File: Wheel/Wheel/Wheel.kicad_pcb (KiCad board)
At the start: 2 copper layers, 122 parts, among them J1 Conn_02x09_Odd_Even, J10 RJ45, J11 Screw_Terminal_01x02, J12 DS-201, J13 Conn_01x04, J14 Conn_02x13_Top_Bottom, J15 DB25_Female, J16 Conn_01x06, J17 Conn_01x07, J18 Conn_01x05, J19 RJ45, J2 RJ45, J20 DB9_Male, J21 DB9_Female, J3 RJ45, J4 RJ45, J5 USB_B, J6 Conn_02x09_Odd_Even, J7 Conn_02x10_Odd_Even, J8 RJ45, J9 RJ45, U1 MCP23S17_SP, U10 PC817, U11 PC817, U12 IP4220CZ6, U13 IP4220CZ6, U14 LTC2644, U15 PC817, U16 IP4220CZ6, U17 IP4220CZ6, U2 STM32F407VETx, U3 USBLC6-2SC6, U4 IP4220CZ6, U5 IP4220CZ6, U6 AMS1117, U7 4N35, U8 PC817, U9 PC817, Y2 8MHz

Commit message: I've modified wheel's PCB
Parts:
- removed C24, C26: 104, Capacitor_SMD:C_0805_2012Metric
- removed U14: LTC2644, Package_SO:MSOP-12_3x4mm_P0.65mm
- added JP1: SolderJumper_2_Bridged, Jumper:SolderJumper-2_P1.3mm_Bridged_RoundedPad1.0x1.5mm, B.Cu at (120.7, 108.0)
- added N1: G313, cases:CASE_G313, F.Cu at (25.5, 19.5)
- C11, C13, C14, C17, JP6: moved to B.Cu
- moved D4 226.4 mm to (32.4, 65.0), turned to 270 degrees
- moved R5 225.3 mm to (37.5, 65.1), turned to 90 degrees
- moved J8 218.6 mm to (42.6, 48.1), turned to 270 degrees
- moved D5 212.8 mm to (32.4, 89.8), turned to 270 degrees
- moved R11 211.7 mm to (37.5, 89.9), turned to 90 degrees
- moved U3 211.6 mm to (70.1, 44.3)
- moved C10 211.6 mm to (59.3, 44.2)
- moved C12 211.6 mm to (55.8, 44.2)
- moved C18 211.6 mm to (60.8, 58.3)
- moved C19 211.6 mm to (55.8, 58.3)
- moved J5 211.6 mm to (62.0, 40.0)
- moved R6 211.6 mm to (64.3, 48.7)
- moved R8 211.6 mm to (71.0, 48.7)
- moved R9 211.6 mm to (67.8, 48.7)
- moved U6 211.6 mm to (58.3, 51.2)
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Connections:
- net Net-(D8-Pad2) renamed PWR_IN
- J14 pad 2: SM1 -> (no net)
- J14 pad 3: PWR -> (no net)
- J14 pad 9: DM1 -> (no net)
- J15 pad 14: SM1 -> (no net)
- J15 pad 5: DM1 -> (no net)
- J15 pad 6: (no net) -> DRIVE_SigIn1
- J18 pad 1: 3V -> GND
- J18 pad 2: GND -> 3V
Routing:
- net PWR: track 64.5 -> 144.9 mm
- net SM1: track 64.6 -> 0.00 mm, vias 2 -> 0
- net DRIVE_PA-: track 27.1 -> 91.7 mm, vias 0 -> 3
- net DRIVE_SigIn1: track 0.00 -> 54.8 mm, vias 0 -> 3
- net DRIVE_PA+: track 24.1 -> 74.8 mm, vias 0 -> 2
- net DM1: track 37.0 -> 0.00 mm, vias 2 -> 0
- net DRIVE_PB+: track 30.3 -> 66.2 mm, vias 0 -> 3
- net DRIVE_PZ-: track 36.5 -> 63.1 mm, vias 0 -> 2
- net DRIVE_PB-: track 33.4 -> 58.1 mm, vias 0 -> 2
- net PWR_IN: track 0.00 -> 23.5 mm
- net DRIVE_VREF: track 77.2 -> 55.7 mm, vias 2 -> 3
- net DRIVE_SigIn2: track 39.1 -> 56.3 mm, vias 2 -> 3
- net PEDAL_BREAK: track 0.00 -> 15.9 mm, vias 0 -> 2
- net DRIVE_PZ+: track 39.6 -> 52.5 mm, vias 0 -> 3
- net Net-(J13-Pad2): track 0.00 -> 12.6 mm
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- added copper zone on B.Cu, net COM
- added copper zone on F.Cu, net COM
- added copper zone on B.Cu, net GND
- added copper zone on F.Cu, net GND
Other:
- board outline added: 188 x 356 mm
- net class DIGITAL: clearance 0.2 -> 0.3
- net class POWER: clearance 0.5 -> 0.3
- board text added: "G1208"

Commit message: TDD Wheel's was changed
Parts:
- removed C16, C22, C27, C28: 104, Capacitor_SMD:C_0805_2012Metric
- removed R12: 330, Resistor_SMD:R_0805_2012Metric
- removed U13, U16, U17: IP4220CZ6, Package_SO:TSOP-6_1.65x3.05mm_P0.95mm
- added C3: 6pF, Capacitor_SMD:C_0805_2012Metric, F.Cu at (106.7, 68.3)
- added C4: 6pF, Capacitor_SMD:C_0805_2012Metric, F.Cu at (106.7, 60.6)
- added R4: 10M, Resistor_SMD:R_0805_2012Metric, F.Cu at (106.7, 64.4)
- added R7: 330, Resistor_SMD:R_0805_2012Metric, F.Cu at (37.5, 89.9)
- added Y1: 32,768 кГц, Crystal:Crystal_C26-LF_D2.1mm_L6.5mm_Horizontal_1EP_style2, F.Cu at (108.6, 65.4)
- C13: moved to F.Cu
- C15, C21, R6, U12, U4: moved to B.Cu
- D8: value 1N4003 -> 1N5818
- J1, J6: footprint Connector_PinHeader_2.54mm:PinHeader_2x09_P2.54mm_Vertical -> Connector_PinHeader_2.54mm:PinHeader_1x18_P2.54mm_Vertical
- J18: value Conn_01x05 -> Conn_01x06; footprint Connector_PinHeader_2.54mm:PinHeader_1x05_P2.54mm_Vertical -> Connector_PinHeader_2.54mm:PinHeader_1x06_P2.54mm_Vertical
- R26: value 330 -> 560
- U10, U11, U15, U8, U9: footprint Package_DIP:DIP-4_W7.62mm -> Package_DIP:SMDIP-4_W7.62mm
- U5: value IP4220CZ6 -> MCP23S17_SP; footprint Package_SO:TSOP-6_1.65x3.05mm_P0.95mm -> Package_DIP:DIP-28_W7.62mm
- U7: footprint Package_DIP:DIP-6_W7.62mm -> Package_DIP:SMDIP-6_W7.62mm
- moved N1 214.6 mm to (240.0, 26.7)
- moved J7 36.8 mm to (109.9, 92.7)
- moved J16 31.1 mm to (73.7, 85.1), turned to 180 degrees
- moved U1 29.9 mm to (114.3, 58.4), turned to 90 degrees
- moved R11 24.8 mm to (37.5, 114.7)
- moved U5 23.8 mm to (64.8, 105.4), turned to 180 degrees
- moved C11 18.7 mm to (140.7, 54.6), turned to 0 degrees
- moved J18 17.8 mm to (89.5, 120.0), turned to 90 degrees
- moved J1 16.1 mm to (157.5, 45.7)
- moved C13 14.9 mm to (69.2, 84.1), turned to 90 degrees
- moved U4 10.6 mm to (66.6, 114.6)
- moved C8 8.84 mm to (93.5, 65.6)
- moved C5 8.84 mm to (100.8, 65.6)
- moved R10 8.84 mm to (97.2, 65.6)
- moved Y2 8.84 mm to (99.4, 61.4)
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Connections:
- net CS0 renamed CS
- J10 pad 2: BTN13 -> /B29
- J10 pad 3: BTN14 -> /B30
- J10 pad 4: BTN15 -> /B31
- J10 pad 5: BTN16 -> /B32
- J16 pad 1: SPI1_CS -> 3V
- J16 pad 2: SPI1_SCK -> GND
- J16 pad 3: SPI1_MISO -> SPI1_CS
- J16 pad 4: SPI1_MOSI -> SPI1_SCK
- J16 pad 5: 3V -> SPI1_SI
- J16 pad 6: GND -> SPI1_SO
- J17 pad 1: SPI1_SCK -> GND
- J17 pad 2: GND -> 3V
- J17 pad 3: SPI1_MISO -> SPI1_SCK
- J17 pad 4: 3V -> SPI1_SO
- J17 pad 6: SHIFTER_Y -> SHIFTER_X
- J17 pad 7: SHIFTER_X -> SHIFTER_Y
- J18 pad 1: GND -> Net-(J18-Pad1)
- J18 pad 2: 3V -> GND
- J18 pad 3: PEDAL_GAS -> 3V
- J18 pad 4: PEDAL_BREAK -> PEDAL_CLUCH
- J18 pad 5: PEDAL_CLUCH -> PEDAL_BREAK
- J20 pad 2: SPI1_MISO -> SPI1_SO
- J21 pad 9: Net-(J21-Pad9) -> Net-(J18-Pad1)
- J6 pad 1: BTN1 -> /B17
- J6 pad 10: BTN10 -> /B26
- J6 pad 11: BTN11 -> /B27
- J6 pad 12: BTN12 -> /B28
- J6 pad 13: BTN13 -> /B29
- J6 pad 14: BTN14 -> /B30
- J6 pad 15: BTN15 -> /B31
- J6 pad 16: BTN16 -> /B32
- J6 pad 2: BTN2 -> /B18
- J6 pad 3: BTN3 -> /B19
- J6 pad 4: BTN4 -> /B20
- J6 pad 5: BTN5 -> /B21
- J6 pad 6: BTN6 -> /B22
- J6 pad 7: BTN7 -> /B23
- J6 pad 8: BTN8 -> /B24
- J6 pad 9: BTN9 -> /B25
- J8 pad 2: BTN1 -> /B17
- J8 pad 3: BTN2 -> /B18
- J8 pad 4: BTN3 -> /B19
- J8 pad 5: BTN4 -> /B20
- J8 pad 6: BTN5 -> /B21
- J8 pad 7: BTN6 -> /B22
- J9 pad 2: BTN7 -> /B23
- J9 pad 3: BTN8 -> /B24
- J9 pad 4: BTN9 -> /B25
- J9 pad 5: BTN10 -> /B26
- J9 pad 6: BTN11 -> /B27
- J9 pad 7: BTN12 -> /B28
- JP6 pad 2: Net-(J21-Pad9) -> Net-(J18-Pad1)
- R11 pad 1: Net-(D5-Pad2) -> Net-(D6-Pad2)
- U12 pad 1: SHIFTER_X -> PEDAL_CLUCH
- U12 pad 3: PEDAL_CLUCH -> SHIFTER_Y
- U2 pad 1: BTN3 -> (no net)
- U2 pad 2: BTN4 -> (no net)
- U2 pad 3: BTN5 -> (no net)
- U2 pad 31: SPI1_MISO -> SPI1_SO
- U2 pad 32: SPI1_MOSI -> SPI1_SI
- U2 pad 4: BTN6 -> (no net)
- U2 pad 63: BTN7 -> (no net)
- U2 pad 64: BTN8 -> (no net)
- U2 pad 65: BTN9 -> (no net)
- U2 pad 66: BTN10 -> (no net)
- U2 pad 7: BTN14 -> (no net)
- U2 pad 78: BTN11 -> (no net)
- U2 pad 79: BTN12 -> (no net)
- U2 pad 80: BTN13 -> (no net)
- U2 pad 97: BTN1 -> (no net)
- U2 pad 98: BTN2 -> (no net)
- U4 pad 1: SPI1_MISO -> SPI1_SO
- U4 pad 4: SPI1_CS -> SHIFTER_X
- U4 pad 6: SHIFTER_Y -> SPI1_CS
- U5 pad 1: BTN9 -> /B17
- U5 pad 2: GND -> /B18
- U5 pad 3: BTN10 -> /B19
- U5 pad 4: BTN11 -> /B20
- U5 pad 5: 3V -> /B21
- U5 pad 6: BTN12 -> /B22
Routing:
- net 3V: track 8.24 -> 534.7 mm, vias 0 -> 11
- net /B18: track 0.00 -> 80.3 mm, vias 0 -> 2
- net /B17: track 0.00 -> 78.9 mm, vias 0 -> 1
- net /B8: track 0.00 -> 76.4 mm, vias 0 -> 5
- net /B1: track 0.00 -> 73.7 mm, vias 0 -> 3
- net /B24: track 0.00 -> 73.6 mm, vias 0 -> 5
- net /B4: track 0.00 -> 71.3 mm, vias 0 -> 3
- net /B2: track 0.00 -> 71.2 mm, vias 0 -> 1
- net /B20: track 0.00 -> 70.1 mm, vias 0 -> 2
- net /B19: track 0.00 -> 69.1 mm, vias 0 -> 1
- net /B7: track 0.00 -> 69.0 mm, vias 0 -> 5
- net /B3: track 0.00 -> 57.9 mm, vias 0 -> 1
- net /B21: track 0.00 -> 56.8 mm, vias 0 -> 1
- net /B22: track 0.00 -> 56.7 mm, vias 0 -> 1
- net /B23: track 0.00 -> 55.3 mm, vias 0 -> 3
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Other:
- net class DIGITAL: clearance 0.3 -> 0.5
- net class Default: clearance 0.3 -> 0.4
- net class POWER: clearance 0.3 -> 0.2
- rule trace_clearance: 0.3 -> 0.4

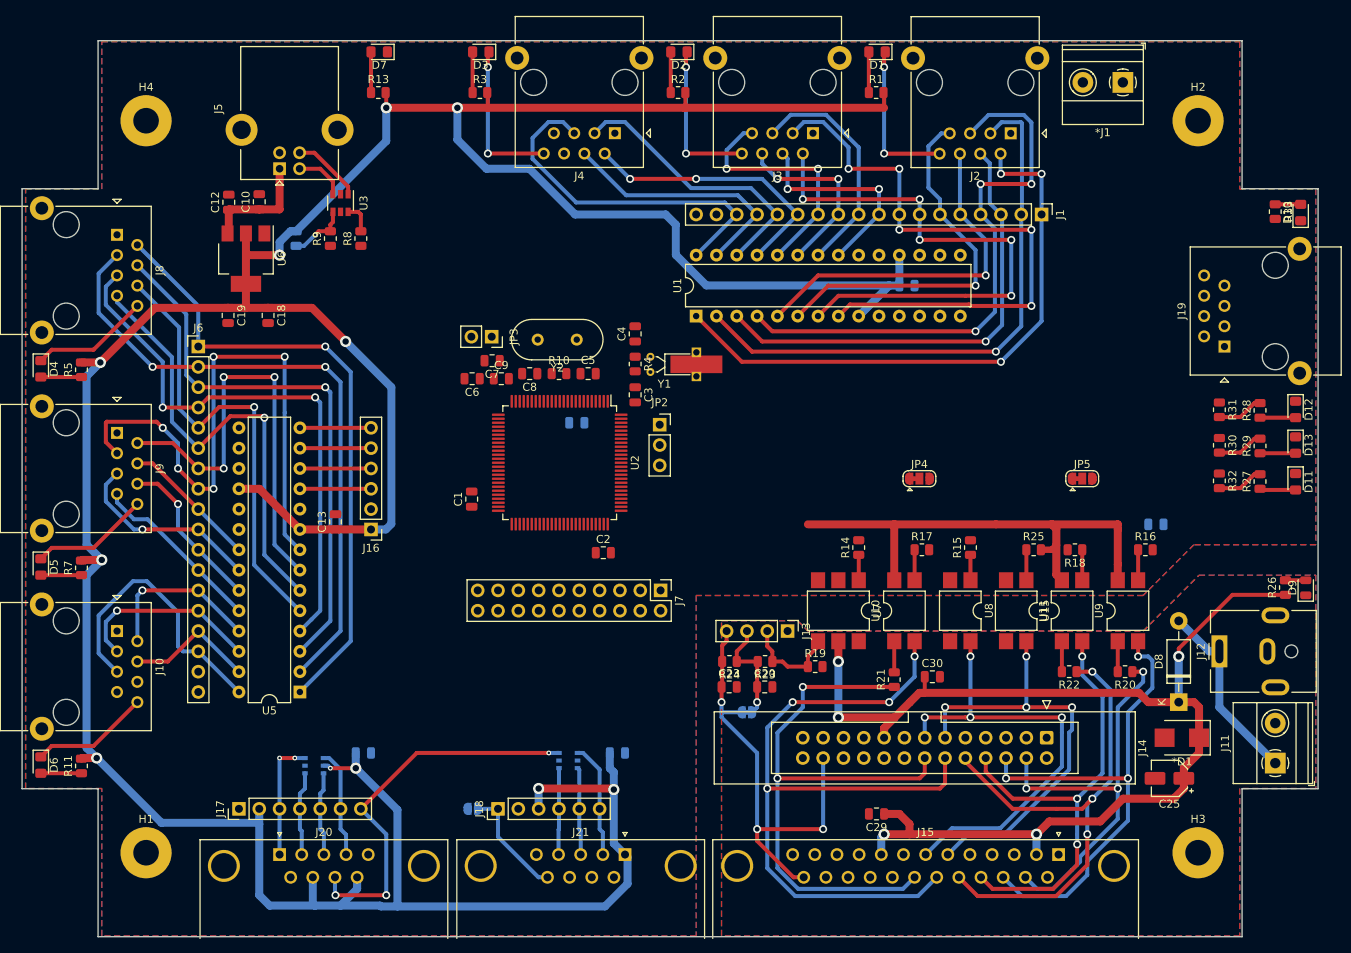
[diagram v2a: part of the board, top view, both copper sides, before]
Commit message: Wheel's PCB changed
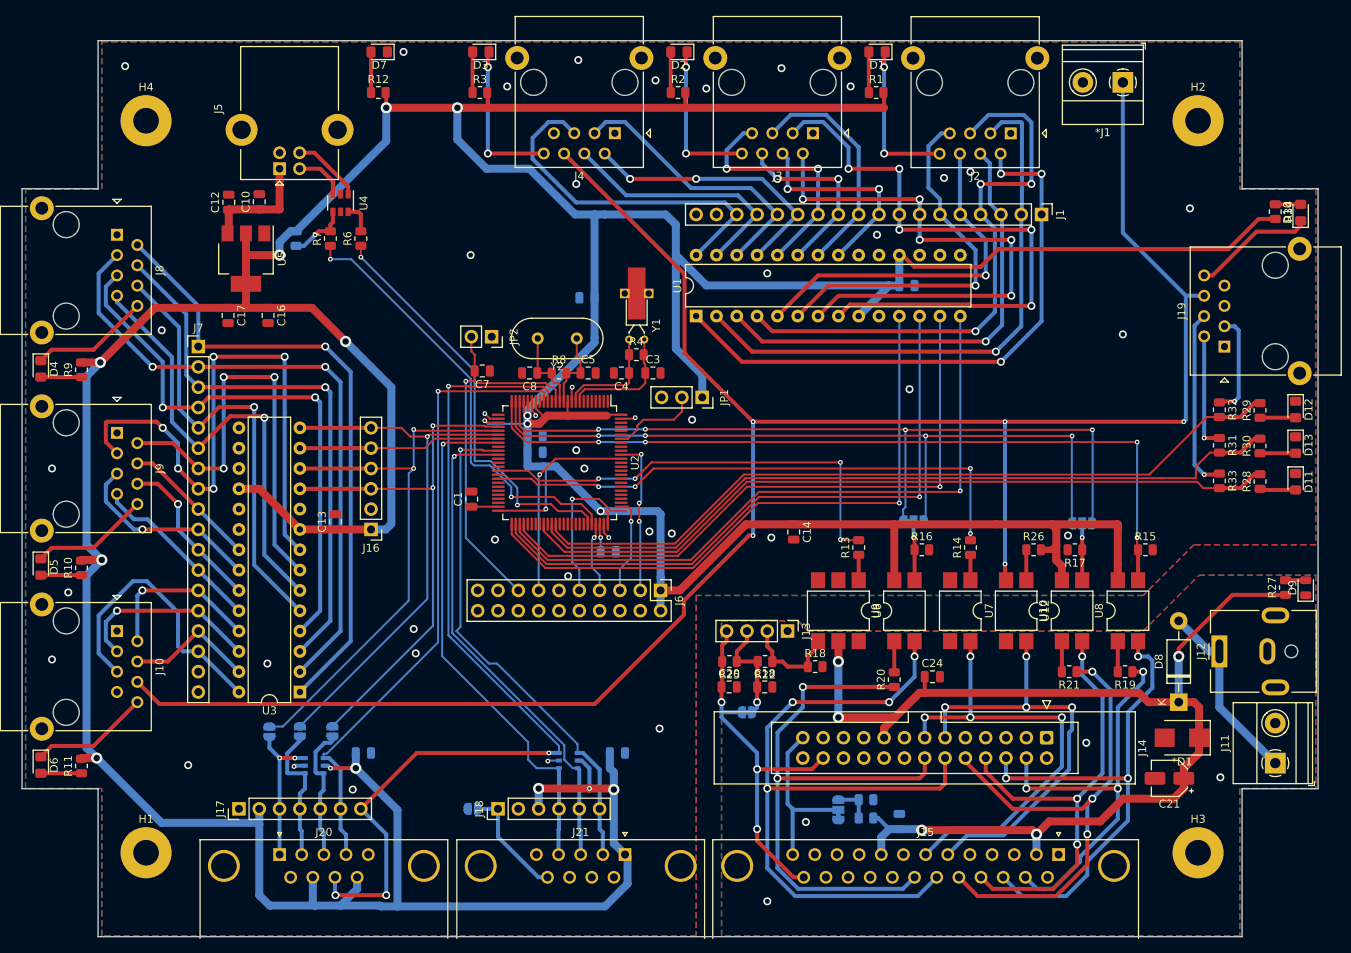
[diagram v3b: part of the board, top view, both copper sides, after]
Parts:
- added JP5: SolderJumper_3_Bridged12, Jumper:SolderJumper-3_P1.3mm_Bridged12_RoundedPad1.0x1.5mm, B.Cu at (132.1, 120.1)
- added JP7: SolderJumper_2_Open, Jumper:SolderJumper-2_P1.3mm_Open_RoundedPad1.0x1.5mm, B.Cu at (68.8, 110.3)
- added JP8: SolderJumper_2_Open, Jumper:SolderJumper-2_P1.3mm_Open_RoundedPad1.0x1.5mm, B.Cu at (64.8, 110.3)
- added JP9: SolderJumper_2_Open, Jumper:SolderJumper-2_P1.3mm_Open_RoundedPad1.0x1.5mm, B.Cu at (61.0, 110.4)
- added R23: 560, Resistor_SMD:R_0805_2012Metric, B.Cu at (135.5, 121.2)
- added R24: 560, Resistor_SMD:R_0805_2012Metric, B.Cu at (135.5, 118.9)
- C14: moved to F.Cu
- C2, C6, C9: moved to B.Cu
- C22: renamed from C29; moved to B.Cu
- JP3: renamed from JP4; moved to B.Cu
- JP4: renamed from JP5; moved to B.Cu
- moved C14 45.3 mm to (126.5, 85.4), turned to 270 degrees
- moved C15 15.7 mm to (100.7, 56.1), turned to 180 degrees
- moved C6 12.1 mm to (94.2, 75.4), turned to 0 degrees
- moved C9 8.31 mm to (94.2, 73.4)
- moved JP1 6.32 mm to (115.1, 68.6), turned to 270 degrees
- moved JP4 5.59 mm to (162.6, 84.3)
- moved JP3 5.38 mm to (141.5, 84.1)
- moved C4 5.18 mm to (105.0, 65.5), turned to 180 degrees
- moved Y1 4.13 mm to (107.8, 61.3), turned to 180 degrees
- moved C3 3.52 mm to (108.9, 65.5), turned to 0 degrees
- moved C22 3.01 mm to (139.7, 121.6), turned to 90 degrees
- moved C7 1.77 mm to (87.6, 65.3)
- moved R4 1.18 mm to (106.8, 63.2), turned to 0 degrees
- moved C2 0.63 mm to (103.3, 87.9)
- moved Y2 0.15 mm to (99.4, 61.2)
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- renumbered C17 to C15, C18 to C16, C19 to C17, C20 to C18, C15 to C19, C23 to C20, C25 to C21, C21 to C23, C30 to C24, J7 to J6, J6 to J7, JP2 to JP1, JP6 to JP10, JP3 to JP2, JP1 to JP6, R7 to R10, R13 to R12, R14 to R13, R15 to R14, R16 to R15, R17 to R16, R18 to R17, R19 to R18, R20 to R19, R21 to R20, R22 to R21, R23 to R22, R24 to R25, R25 to R26, R26 to R27, R27 to R28, R28 to R29, R29 to R30, R30 to R31, R31 to R32, R32 to R33, R33 to R34, R6 to R5, R8 to R6, R9 to R7, R10 to R8, R5 to R9, U11 to U10, U4 to U11, U15 to U12, U12 to U13, U5 to U3, U3 to U4, U6 to U5, U7 to U6, U8 to U7, U9 to U8, U10 to U9
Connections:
- J14 pad 25: COM -> Net-(J14-Pad25)
- J15 pad 13: COM -> Net-(J14-Pad25)
- J17 pad 3: SPI1_SCK -> SPI1_SCK_PROT
- J17 pad 4: SPI1_SO -> SPI1_SO_PROT
- J17 pad 5: SPI1_CS -> SPI1_CS_PROT
- J20 pad 1: SPI1_SCK -> SPI1_SCK_PROT
- J20 pad 2: SPI1_SO -> SPI1_SO_PROT
- J20 pad 3: SPI1_CS -> SPI1_CS_PROT
- U11 pad 1: SPI1_SO -> SPI1_SO_PROT
- U11 pad 3: SPI1_SCK -> SPI1_SCK_PROT
- U11 pad 6: SPI1_CS -> SPI1_CS_PROT
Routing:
- net DRIVE_ENABLE: track 0.00 -> 267.2 mm, vias 0 -> 5
- net 3V: track 534.7 -> 738.4 mm, vias 11 -> 17
- net ENC_A: track 0.00 -> 98.4 mm, vias 0 -> 4
- net ENC_I: track 3.81 -> 99.6 mm, vias 0 -> 4
- net ENC_B: track 0.00 -> 94.9 mm, vias 0 -> 4
- net FORCE_LED_R: track 5.80 -> 96.9 mm
- net FORCE_LED_B: track 5.80 -> 96.8 mm
- net FORCE_LED_G: track 5.80 -> 96.2 mm
- net SO: track 0.00 -> 82.9 mm, vias 0 -> 1
- net SCK: track 0.00 -> 79.3 mm, vias 0 -> 1
- net SI: track 0.00 -> 79.1 mm, vias 0 -> 1
- net CS: track 0.00 -> 78.2 mm, vias 0 -> 1
- net DRV_DIR: track 0.00 -> 69.4 mm, vias 0 -> 4
- net SHIFTER_X: track 13.6 -> 80.1 mm, vias 0 -> 1
- net SHIFTER_Y: track 48.4 -> 113.9 mm, vias 3 -> 4
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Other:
- net class Default: clearance 0.4 -> 0.3
- rule trace_clearance: 0.4 -> 0.3

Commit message: I've modify TDD's PCB.
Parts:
- moved N1 214.8 mm to (25.4, 19.4)
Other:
- board size 188 x 356 mm -> 162 x 112 mm
- board text added: "3V"
- board text added: "3v"
- board text added: "AGND"
- board text added: "B"
- board text added: "BOOT"
- board text added: "BUTTONS 1..6"
- board text added: "BUTTONS 13..16"
- board text added: "BUTTONS 17..22"
- board text added: "BUTTONS 23..28"
- board text added: "BUTTONS 29..32"
- board text added: "BUTTONS 7..12"
- board text added: "C"
- board text added: "COM"
- board text added: "DRIVE"
- board text added: "Designed in Russia"
- board text added: "E-STOP"
- board text added: "FORCE LEDS"
- board text added: "G"
- board text added: "GND"
- board text added: "INDEX / CLIP"
- board text added: "INDICATION"
- board text added: "INDICATION RJ45 1 - GND 2 - FORCE LED RED 3 - LED INDEX 4 - FORCE LED GREEN 6 - E-STOP 8 - INDICATION (8 pin should be connect to 1 pin)"
- board text added: "PA+"
- board text added: "PA-"
- board text added: "PB+"
- board text added: "PB-"
- board text added: "PEDALS"
- board text added: "POWER"
- board text added: "PRG"
- board text added: "PWR"
- board text added: "PZ+"
- board text added: "PZ-"
- board text added: "RESET"
- board text added: "RJ45 1 - GND 2 - BTN1 3 - BTN2 4 - BTN3 5 - BTN4 6 - BTN5 7 - BTN6 8 - INDICATION"
- board text added: "SHIFTER"
- board text added: "Schematics and PCB designed by Yakovlev Yuri <krotos139> Evgeniy Komarov 6DOF-Rotary-Stewart-Motion-Simulator Date: 08.01.2021 ver 1.0"
- board text added: "SigIn1"
- board text added: "SigIn2"
- board text added: "TDD AASD servo MMOS wheel"
- board text added: "USB"
- board text added: "VREF"
- board text added: "X"
- board text added: "Y"
- board text removed: "G1208"

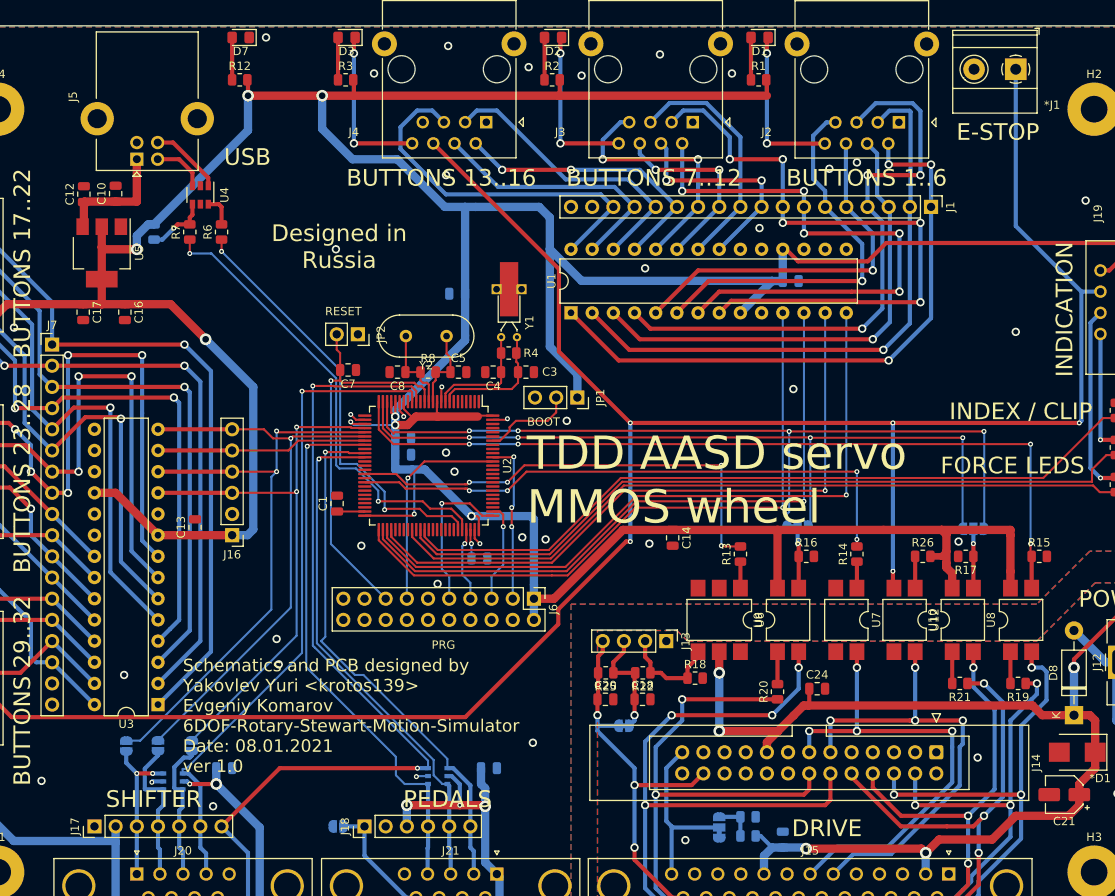
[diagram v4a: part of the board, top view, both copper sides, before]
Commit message: TDD's PCB was changed
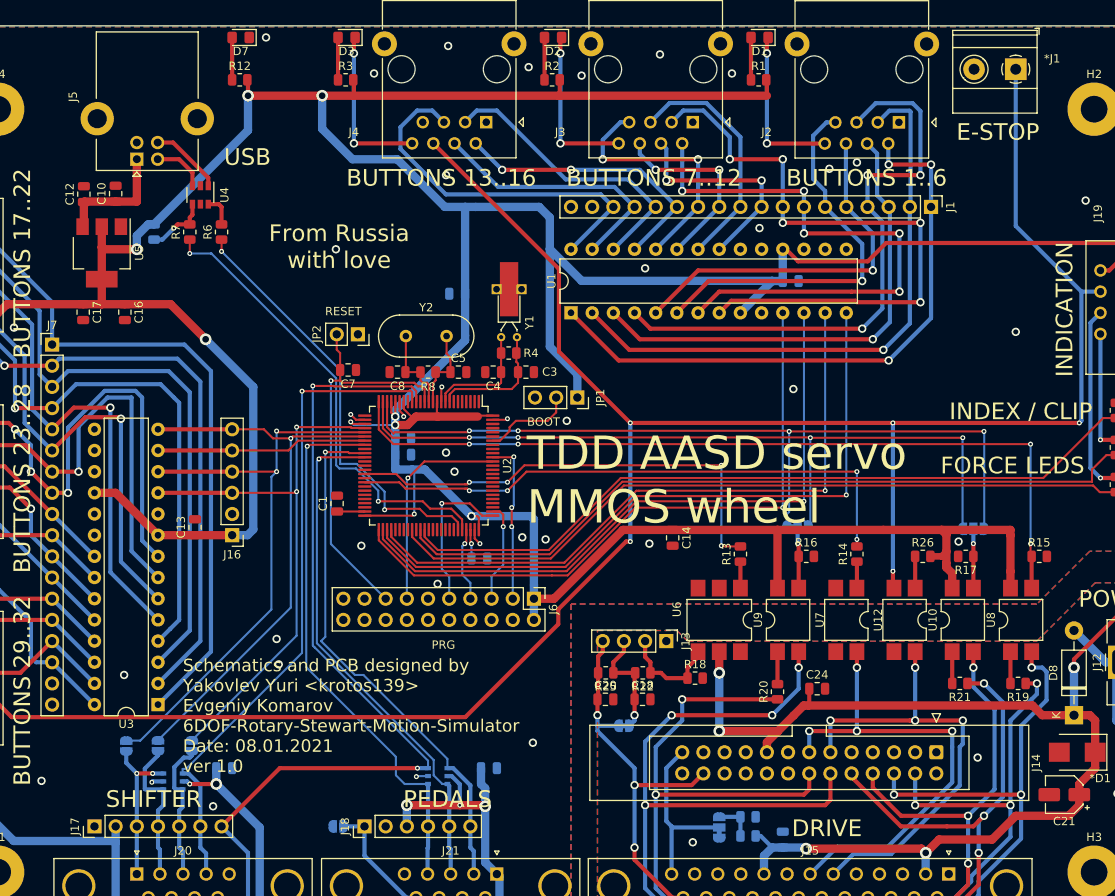
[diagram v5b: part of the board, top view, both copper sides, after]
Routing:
- net /B24: track 73.6 -> 62.0 mm, vias 5 -> 3
- net /B23: track 55.3 -> 48.2 mm, vias 3 -> 1
- net /B19: track 69.1 -> 70.7 mm, vias 1 -> 0
- net /B20: track 70.1 -> 71.5 mm, vias 2 -> 1
- net /B18: track 80.3 -> 81.0 mm, vias 2 -> 1
- net /B17: vias 1 -> 0
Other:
- net class Default: clearance 0.3 -> 0.2
- rule trace_clearance: 0.3 -> 0.2
- board text added: "From Russia with love"
- board text removed: "Designed in Russia"
